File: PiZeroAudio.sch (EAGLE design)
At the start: 64 parts, among them CON1 RPI-ZERO, J1 GROVE, J2 2X2HEADER, J3 2X1-LOCKING, J4 4X1-LOCKING, Q1 DMG2305UX, U1 TXB0104PWR, U2 LSM6DS33, U3 NC7WZ16, U4 DMMT5401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

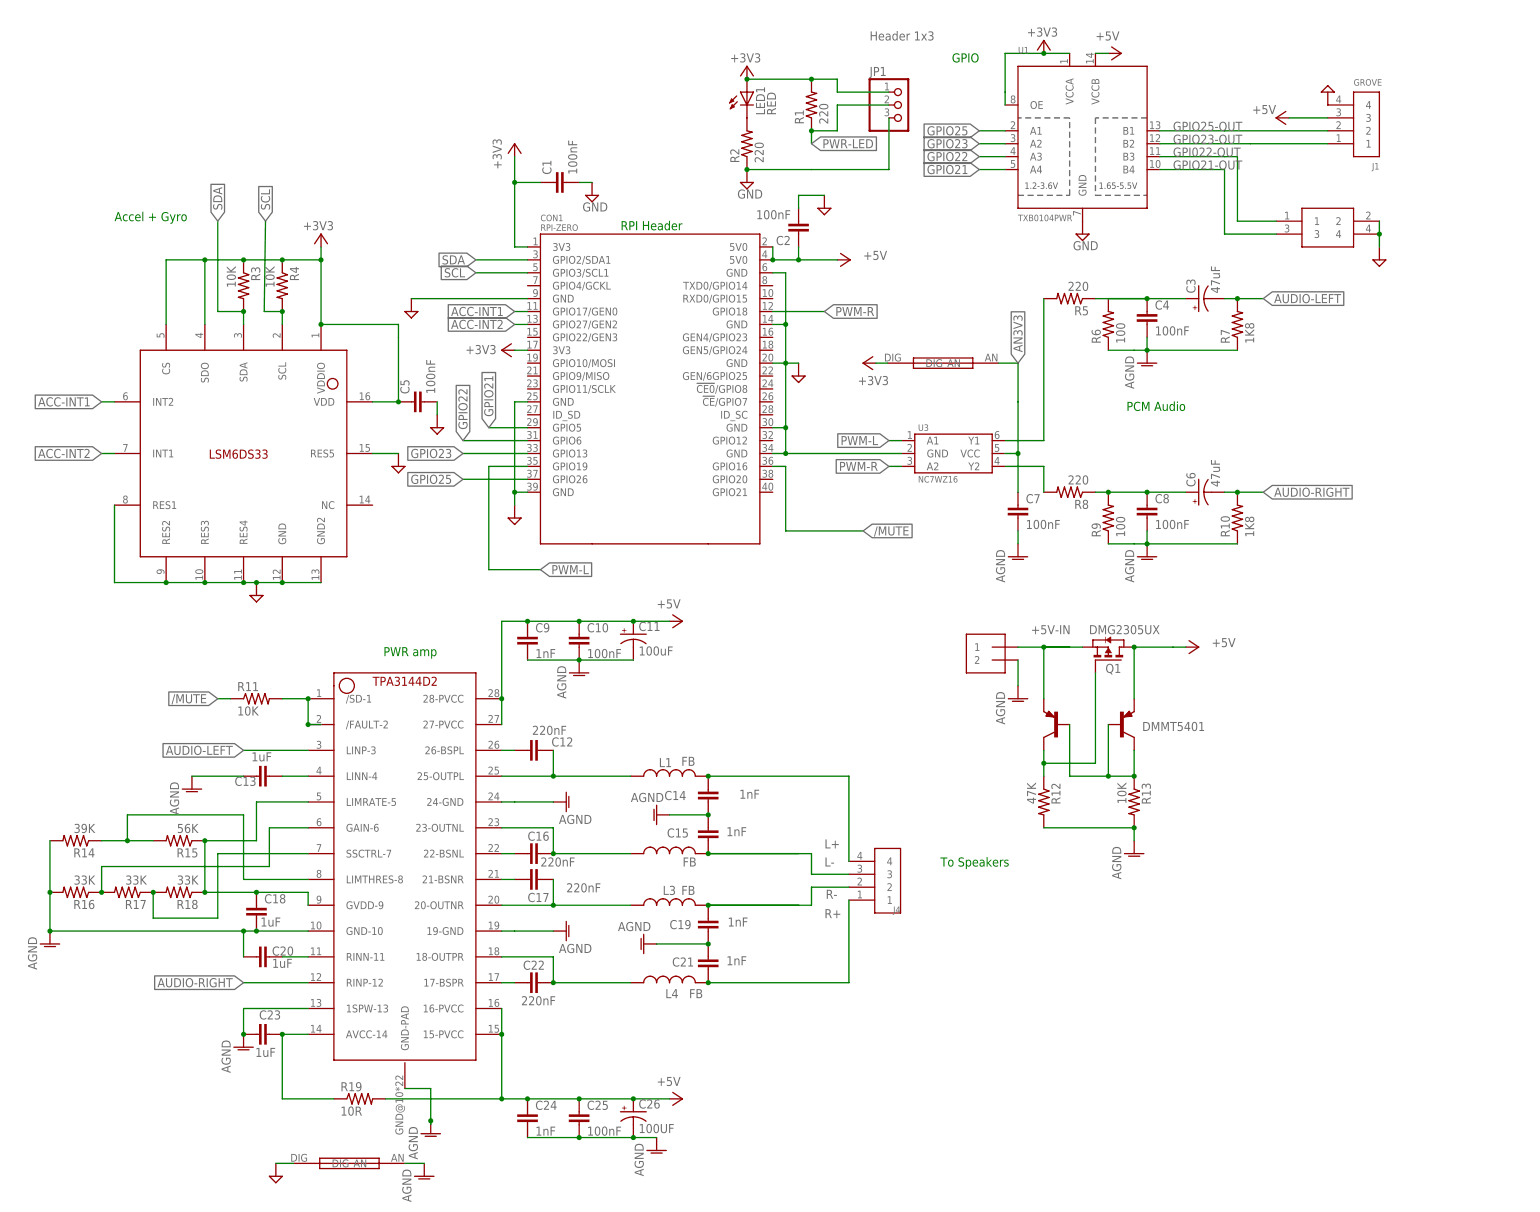
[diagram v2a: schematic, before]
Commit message: added i2C
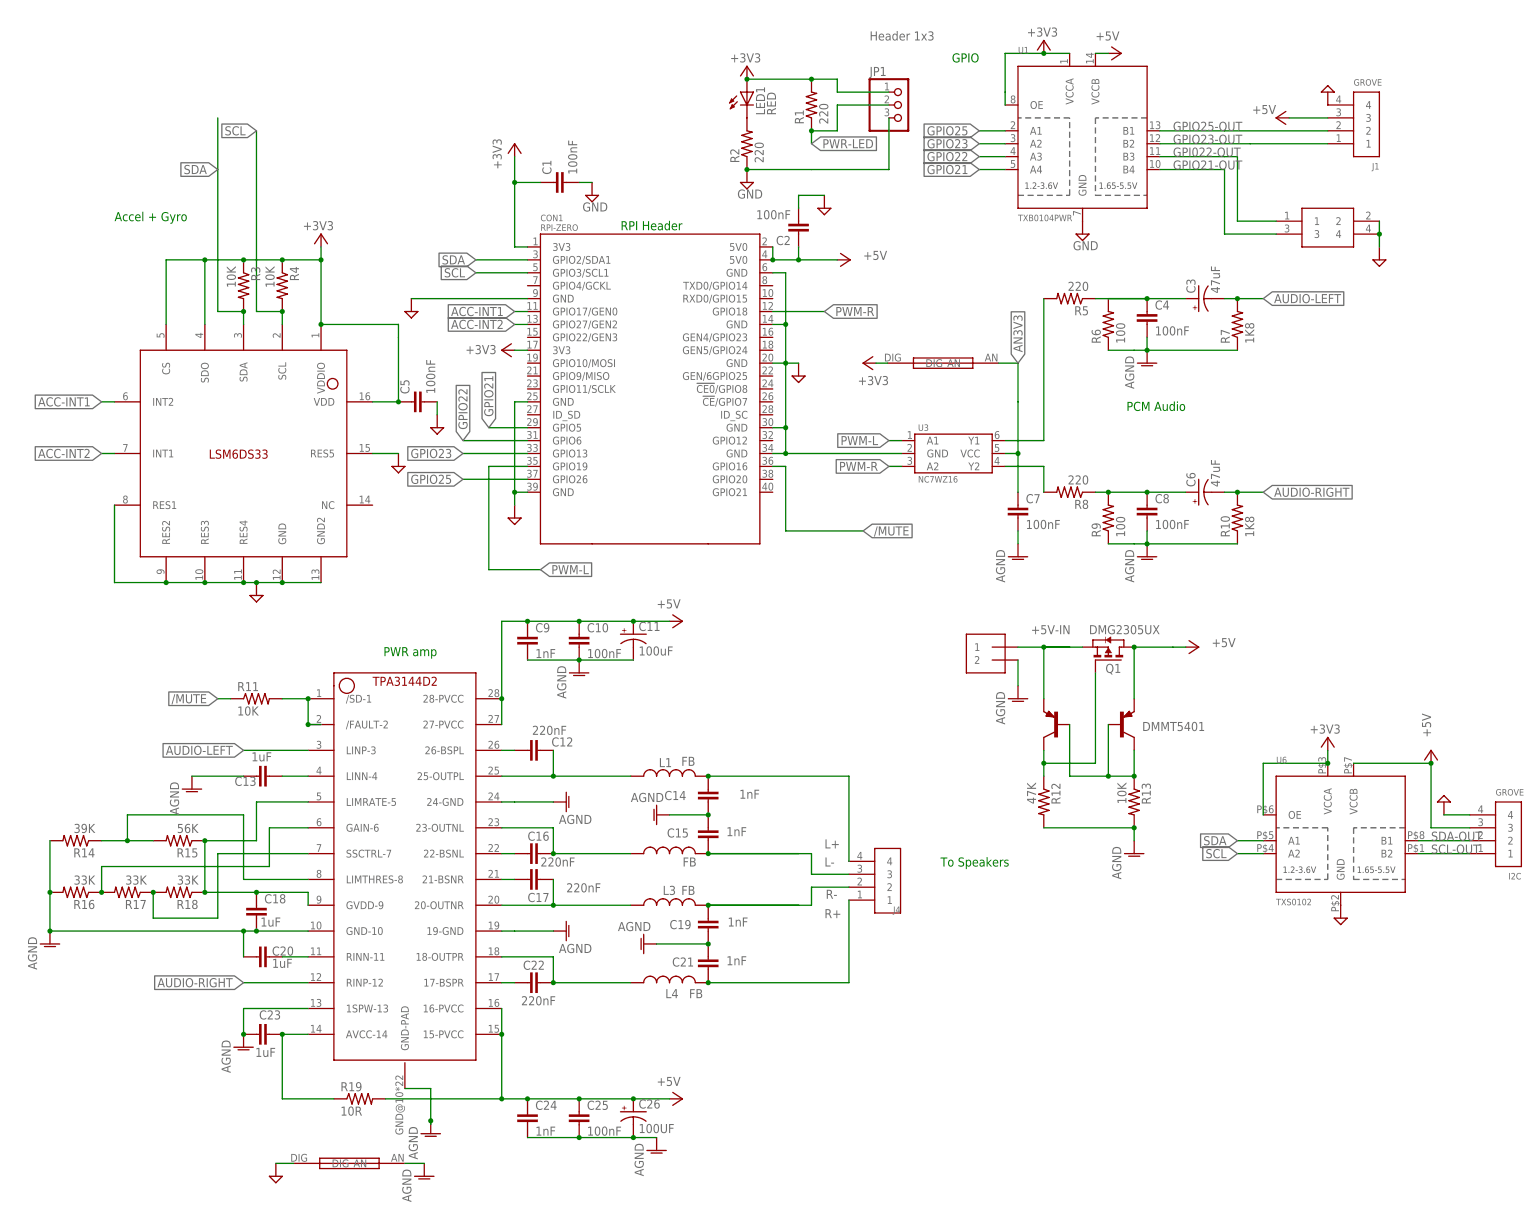
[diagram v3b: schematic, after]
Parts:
- added I2C: GROVE, HappyBrackets:GROVE
- added U6: TXS0102, adafruit:TXS0102
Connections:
- new net SCL-OUT: I2C.1, U6.B2
- new net SDA-OUT: I2C.2, U6.B1
- net +3V3: now also U6.OE, U6.VCCA
- net +5V: now also I2C.3, U6.VCCB
- net GND: now also I2C.4, U6.GND
- net SCL: now also U6.A2
- net SDA: now also U6.A1
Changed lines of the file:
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@@
 <part name="J2" library="HappyBrackets" library_urn="urn:adsk.eagle:library:5224691" deviceset="2X2HEADER" device=""/>
 <part name="P+2" library="supply1" library_urn="urn:adsk.eagle:library:371" deviceset="+5V" device=""/>
+<part name="I2C" library="HappyBrackets" library_urn="urn:adsk.eagle:library:5224691" deviceset="GROVE" device=""/>
+<part name="+3V1" library="supply1" library_urn="urn:adsk.eagle:library:371" deviceset="+3V3" device=""/>
+<part name="SUPPLY14" library="supply2" library_urn="urn:adsk.eagle:library:372" deviceset="GND" device=""/>
+<part name="U6" library="adafruit" deviceset="TXS0102" device="" value="TXS0102"/>
+<part name="P+7" library="supply1" library_urn="urn:adsk.eagle:library:371" deviceset="+5V" device=""/>
+<part name="SUPPLY15" library="supply2" library_urn="urn:adsk.eagle:library:372" deviceset="GND" device=""/>
 </parts>
 <sheets>
@@
 <attribute name="VALUE" x="-241.3" y="226.06" size="1.778" layer="96" rot="R180"/>
 </instance>
+<instance part="I2C" gate="G$1" x="-198.12" y="81.28" rot="MR180"/>
+<instance part="+3V1" gate="G$1" x="-231.14" y="101.6" smashed="yes">
+<attribute name="VALUE" x="-228.6" y="104.14" size="1.778" layer="96" rot="R180"/>
+</instance>
+<instance part="SUPPLY14" gate="GND" x="-208.28" y="88.9" smashed="yes" rot="R180"/>
+<instance part="U6" gate="G$1" x="-228.6" y="83.82"/>
+<instance part="P+7" gate="1" x="-210.82" y="99.06" smashed="yes">
+<attribute name="VALUE" x="-210.82" y="101.6" size="1.778" layer="96" rot="R90"/>
+</instance>
+<instance part="SUPPLY15" gate="GND" x="-228.6" y="66.04" smashed="yes"/>
 </instances>
 <busses>
@@
 <junction x="-220.98" y="200.66"/>
 </segment>
+<segment>
+<pinref part="I2C" gate="G$1" pin="4"/>
+<pinref part="SUPPLY14" gate="GND" pin="GND"/>
+<wire x1="-203.2" y1="86.36" x2="-208.28" y2="86.36" width="0.1524" layer="91"/>
+</segment>
+<segment>
+<pinref part="U6" gate="G$1" pin="GND"/>
+<pinref part="SUPPLY15" gate="GND" pin="GND"/>
+</segment>
 </net>
 <net name="PWM-R" class="0">
@@
 <pinref part="P+2" gate="1" pin="+5V"/>
 <wire x1="-238.76" y1="223.52" x2="-231.14" y2="223.52" width="0.1524" layer="91"/>
+</segment>
+<segment>
+<pinref part="U6" gate="G$1" pin="VCCB"/>
+<wire x1="-226.06" y1="96.52" x2="-210.82" y2="96.52" width="0.1524" layer="91"/>
+<wire x1="-210.82" y1="96.52" x2="-210.82" y2="83.82" width="0.1524" layer="91"/>
+<pinref part="I2C" gate="G$1" pin="3"/>
+<wire x1="-210.82" y1="83.82" x2="-203.2" y2="83.82" width="0.1524" layer="91"/>
+<pinref part="P+7" gate="1" pin="+5V"/>
+<junction x="-210.82" y="96.52"/>
 </segment>
 </net>
@@
 <wire x1="-327.66" y1="228.6" x2="-317.5" y2="228.6" width="0.1524" layer="91"/>
 </segment>
+<segment>
+<pinref part="U6" gate="G$1" pin="VCCA"/>
+<pinref part="+3V1" gate="G$1" pin="+3V3"/>
+<wire x1="-231.14" y1="99.06" x2="-231.14" y2="96.52" width="0.1524" layer="91"/>
+<pinref part="U6" gate="G$1" pin="OE"/>
+<wire x1="-243.84" y1="86.36" x2="-243.84" y2="96.52" width="0.1524" layer="91"/>
+<wire x1="-243.84" y1="96.52" x2="-231.14" y2="96.52" width="0.1524" layer="91"/>
+<junction x="-231.14" y="96.52"/>
+</segment>
 </net>
 <net name="SDA" class="0">
@@
 <pinref part="U2" gate="G$1" pin="SDA"/>
 <wire x1="-444.5" y1="185.42" x2="-444.5" y2="182.88" width="0.1524" layer="91"/>
-<label x="-449.58" y="203.2" size="1.778" layer="95" rot="R90" xref="yes"/>
-<wire x1="-449.58" y1="203.2" x2="-449.58" y2="185.42" width="0.1524" layer="91"/>
+<label x="-449.58" y="213.36" size="1.778" layer="95" rot="R180" xref="yes"/>
+<wire x1="-449.58" y1="213.36" x2="-449.58" y2="185.42" width="0.1524" layer="91"/>
 <wire x1="-449.58" y1="185.42" x2="-444.5" y2="185.42" width="0.1524" layer="91"/>
 <junction x="-444.5" y="185.42"/>
+<wire x1="-449.58" y1="213.36" x2="-449.58" y2="223.52" width="0.1524" layer="91"/>
+</segment>
+<segment>
+<pinref part="U6" gate="G$1" pin="A1"/>
+<wire x1="-243.84" y1="81.28" x2="-248.92" y2="81.28" width="0.1524" layer="91"/>
+<label x="-248.92" y="81.28" size="1.778" layer="95" rot="R180" xref="yes"/>
 </segment>
 </net>
@@
 <pinref part="U2" gate="G$1" pin="SCL"/>
 <wire x1="-436.88" y1="185.42" x2="-436.88" y2="182.88" width="0.1524" layer="91"/>
-<label x="-440.182" y="203.2" size="1.778" layer="95" rot="R90" xref="yes"/>
-<wire x1="-440.182" y1="203.2" x2="-440.436" y2="185.42" width="0.1524" layer="91"/>
-<wire x1="-440.436" y1="185.42" x2="-436.88" y2="185.42" width="0.1524" layer="91"/>
 <junction x="-436.88" y="185.42"/>
+<wire x1="-441.96" y1="185.42" x2="-436.88" y2="185.42" width="0.1524" layer="91"/>
+<wire x1="-441.96" y1="220.98" x2="-441.96" y2="185.42" width="0.1524" layer="91"/>
+<label x="-441.96" y="220.98" size="1.778" layer="95" rot="R180" xref="yes"/>
+</segment>
+<segment>
+<pinref part="U6" gate="G$1" pin="A2"/>
+<wire x1="-243.84" y1="78.74" x2="-248.92" y2="78.74" width="0.1524" layer="91"/>
+<label x="-248.92" y="78.74" size="1.778" layer="95" rot="R180" xref="yes"/>
 </segment>
 </net>
@@
 </segment>
 </net>
+<net name="SDA-OUT" class="0">
+<segment>
+<pinref part="U6" gate="G$1" pin="B1"/>
+<pinref part="I2C" gate="G$1" pin="2"/>
+<wire x1="-213.36" y1="81.28" x2="-203.2" y2="81.28" width="0.1524" layer="91"/>
+<label x="-210.82" y="81.28" size="1.778" layer="95"/>
+</segment>
+</net>
+<net name="SCL-OUT" class="0">
+<segment>
+<pinref part="I2C" gate="G$1" pin="1"/>
+<pinref part="U6" gate="G$1" pin="B2"/>
+<wire x1="-203.2" y1="78.74" x2="-213.36" y2="78.74" width="0.1524" layer="91"/>
+<label x="-210.82" y="78.74" size="1.778" layer="95"/>
+</segment>
+</net>
